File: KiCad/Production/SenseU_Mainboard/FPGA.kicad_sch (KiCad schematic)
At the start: 3 parts

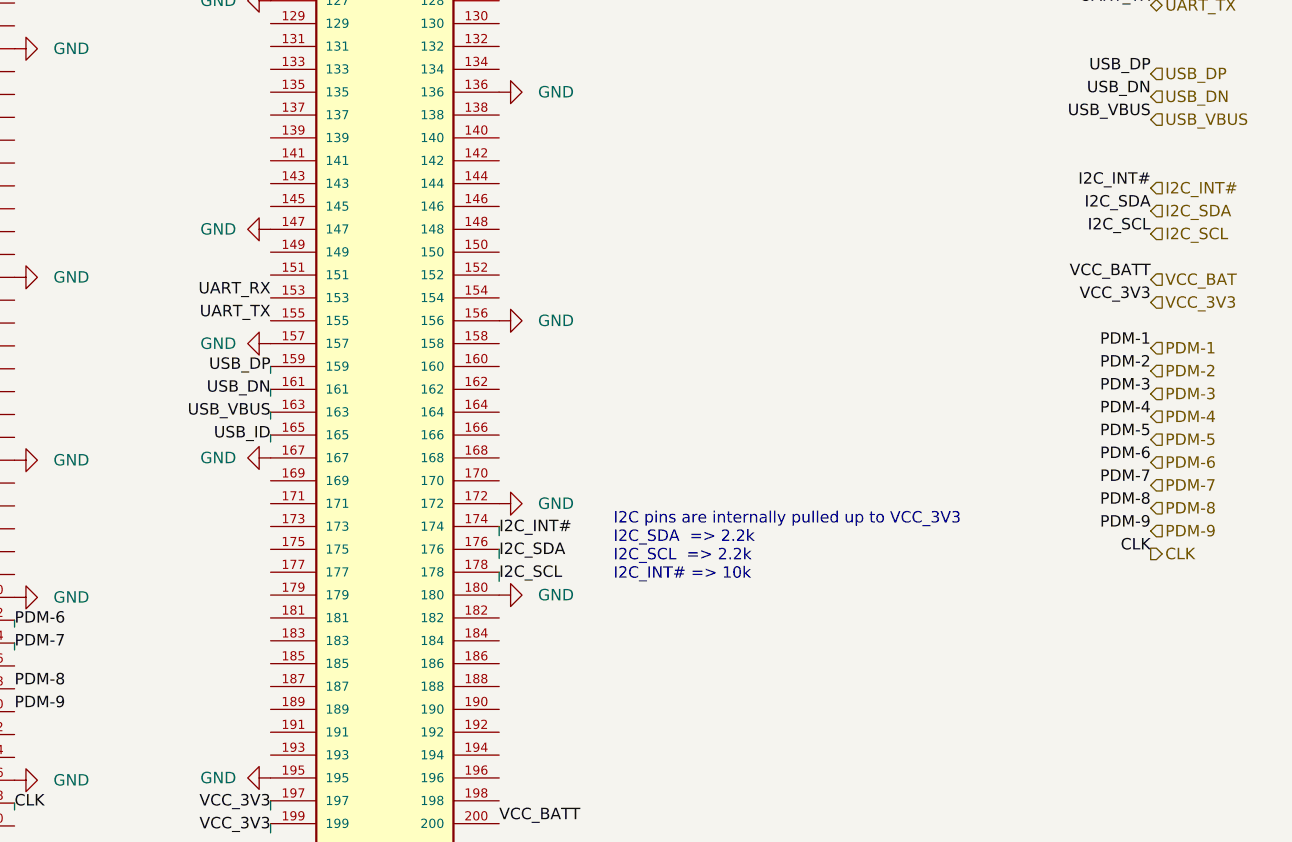
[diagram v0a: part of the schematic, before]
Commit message: added USB TO UART
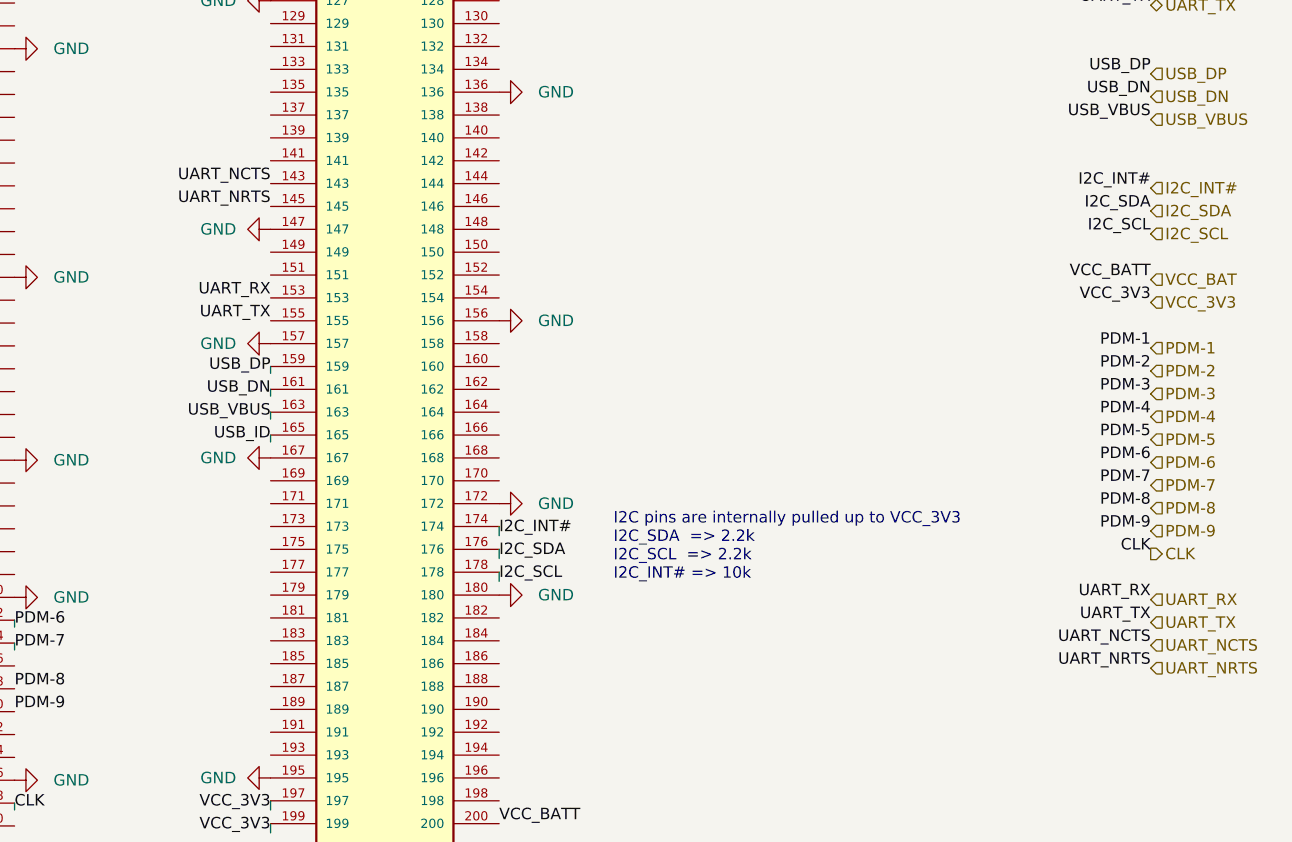
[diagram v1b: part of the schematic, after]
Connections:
- net UART_NCTS: now reaches J?.143
- net UART_NRTS: now reaches J?.145
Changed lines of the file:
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@@
+    (effects (font (size 1.27 1.27)) (justify right bottom))
+  )
+  (label "UART_NRTS" (at 163.83 73.152 180) (fields_autoplaced)
     (effects (font (size 1.27 1.27)) (justify right bottom))
   )
@@
     (effects (font (size 1.27 1.27)) (justify right bottom))
   )
+  (label "UART_TX" (at 261.62 119.38 180) (fields_autoplaced)
+    (effects (font (size 1.27 1.27)) (justify right bottom))
+  )
   (label "VCC_BATT" (at 189.23 141.732 0) (fields_autoplaced)
     (effects (font (size 1.27 1.27)) (justify left bottom))
@@
     (effects (font (size 1.27 1.27)) (justify left bottom))
   )
+  (label "UART_NCTS" (at 261.62 121.92 180) (fields_autoplaced)
+    (effects (font (size 1.27 1.27)) (justify right bottom))
+  )
   (label "VCC_3V3" (at 42.164 77.978 180) (fields_autoplaced)
     (effects (font (size 1.27 1.27)) (justify right bottom))
@@
     (effects (font (size 1.27 1.27)) (justify right bottom))
   )
+  (label "UART_NCTS" (at 163.83 70.612 180) (fields_autoplaced)
+    (effects (font (size 1.27 1.27)) (justify right bottom))
+  )
   (label "USB_ID" (at 163.83 99.314 180) (fields_autoplaced)
     (effects (font (size 1.27 1.27)) (justify right bottom))
@@
     (effects (font (size 1.27 1.27)) (justify right bottom))
   )
+  (label "UART_NRTS" (at 261.62 124.46 180) (fields_autoplaced)
+    (effects (font (size 1.27 1.27)) (justify right bottom))
+  )
   (label "PDM-6" (at 135.382 119.888 0) (fields_autoplaced)
     (effects (font (size 1.27 1.27)) (justify left bottom))
@@
   )
   (label "PDM-9" (at 261.62 109.22 180) (fields_autoplaced)
+    (effects (font (size 1.27 1.27)) (justify right bottom))
+  )
+  (label "UART_RX" (at 261.62 116.84 180) (fields_autoplaced)
     (effects (font (size 1.27 1.27)) (justify right bottom))
   )
@@
     (effects (font (size 1.27 1.27)) (justify left))
   )
+  (hierarchical_label "UART_NCTS" (shape input) (at 261.62 121.92 0) (fields_autoplaced)
+    (effects (font (size 1.27 1.27)) (justify left))
+  )
   (hierarchical_label "PDM-3" (shape input) (at 261.62 93.98 0) (fields_autoplaced)
     (effects (font (size 1.27 1.27)) (justify left))
@@
     (effects (font (size 1.27 1.27)) (justify left))
   )
+  (hierarchical_label "UART_TX" (shape input) (at 261.62 119.38 0) (fields_autoplaced)
+    (effects (font (size 1.27 1.27)) (justify left))
+  )
   (hierarchical_label "PDM-7" (shape input) (at 261.62 104.14 0) (fields_autoplaced)
     (effects (font (size 1.27 1.27)) (justify left))
@@
     (effects (font (size 1.27 1.27)) (justify left))
   )
+  (hierarchical_label "UART_RX" (shape input) (at 261.62 116.84 0) (fields_autoplaced)
+    (effects (font (size 1.27 1.27)) (justify left))
+  )
   (hierarchical_label "UART_RX" (shape bidirectional) (at 261.62 48.26 0) (fields_autoplaced)
     (effects (font (size 1.27 1.27)) (justify left))
@@
     (effects (font (size 1.27 1.27)) (justify left))
   )
+  (hierarchical_label "UART_NRTS" (shape input) (at 261.62 124.46 0) (fields_autoplaced)
+    (effects (font (size 1.27 1.27)) (justify left))
+  )

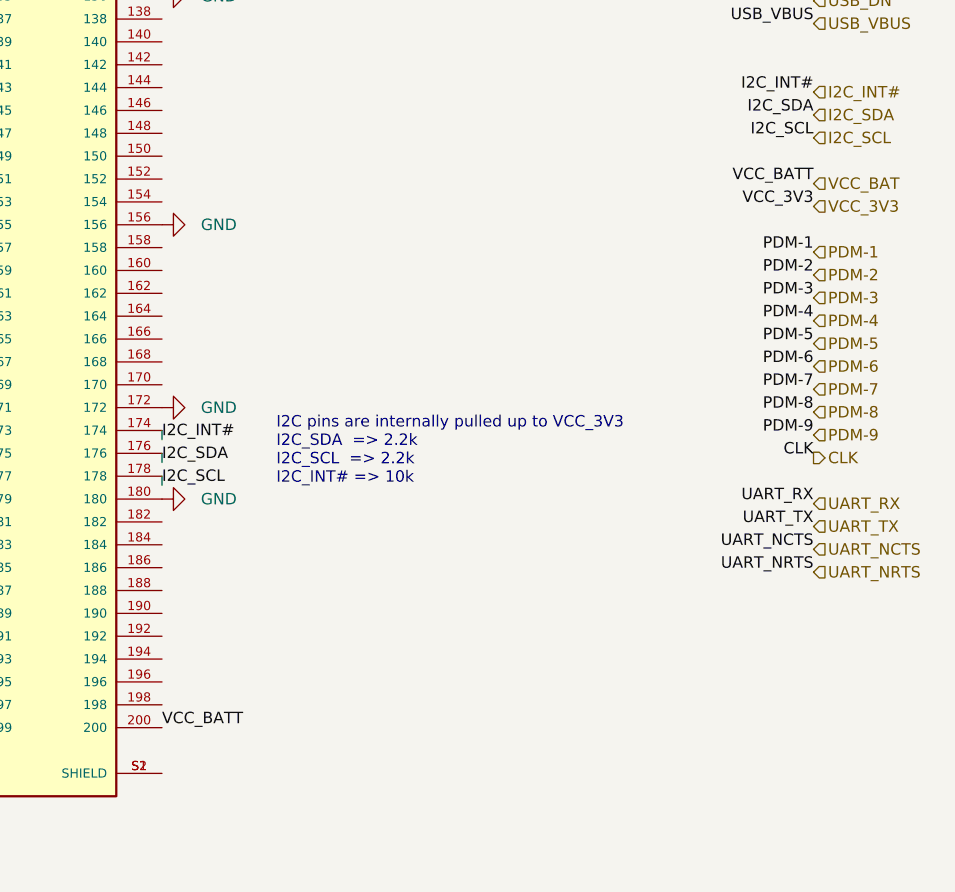
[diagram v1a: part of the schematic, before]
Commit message: removed batt co to fpga and added switch
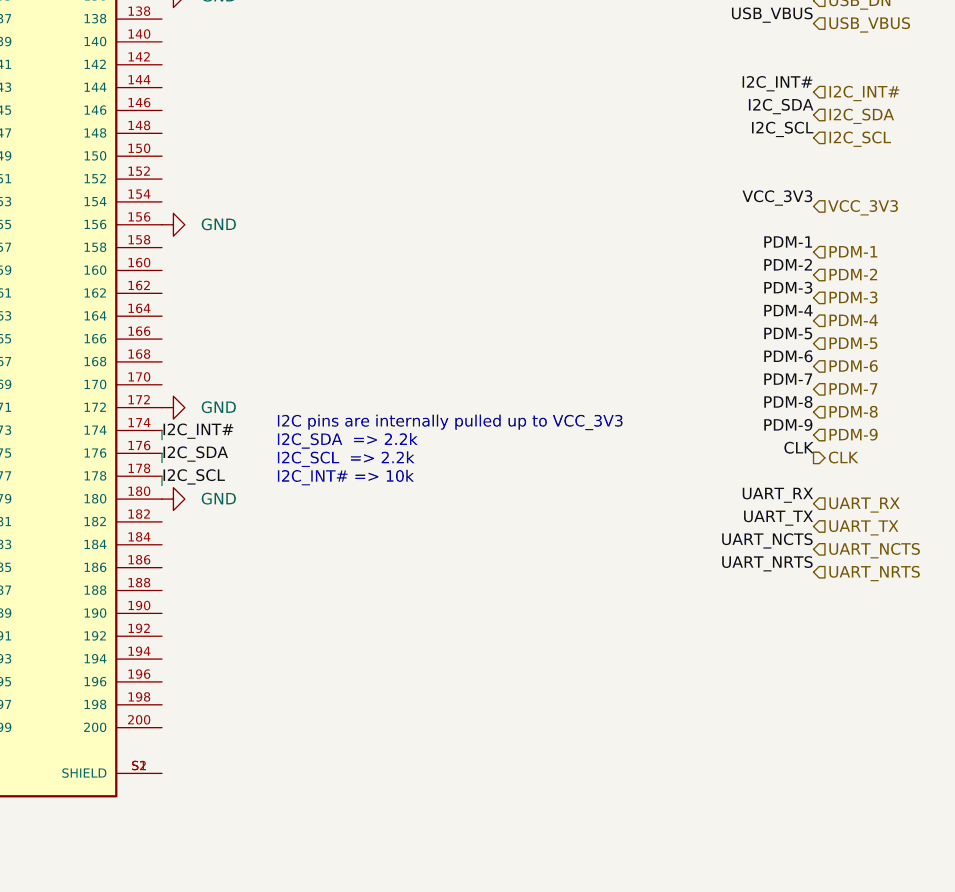
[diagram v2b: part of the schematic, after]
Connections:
- net VCC_BAT: no longer names the net of J?.200
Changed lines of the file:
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@@
     (effects (font (size 1.27 1.27)) (justify right bottom))
-  )
-  (label "VCC_BATT" (at 189.23 141.732 0) (fields_autoplaced)
-    (effects (font (size 1.27 1.27)) (justify left bottom))
   )
   (label "CLK" (at 135.382 140.208 0) (fields_autoplaced)
@@
     (effects (font (size 1.27 1.27)) (justify right bottom))
   )
-  (label "VCC_BATT" (at 261.62 81.28 180) (fields_autoplaced)
-    (effects (font (size 1.27 1.27)) (justify right bottom))
-  )
   (label "CLK" (at 261.62 111.76 180) (fields_autoplaced)
     (effects (font (size 1.27 1.27)) (justify right bottom))
@@
     (effects (font (size 1.27 1.27)) (justify left))
   )
-  (hierarchical_label "VCC_BAT" (shape input) (at 261.62 81.28 0) (fields_autoplaced)
-    (effects (font (size 1.27 1.27)) (justify left))
-  )

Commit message: routing SenseU done
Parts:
- J? (x3): footprint TE_1717254-4 -> Dimm200:TE_1717254-4
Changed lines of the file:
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@@
       (effects (font (size 1.27 1.27)))
     )
-    (property "Footprint" "TE_1717254-4" (at 122.682 91.186 0)
+    (property "Footprint" "Dimm200:TE_1717254-4" (at 122.682 91.186 0)
       (effects (font (size 1.27 1.27)) (justify bottom) hide)
     )
@@
       (effects (font (size 1.27 1.27)))
     )
-    (property "Footprint" "TE_1717254-4" (at 176.53 93.472 0)
+    (property "Footprint" "Dimm200:TE_1717254-4" (at 176.53 93.472 0)
       (effects (font (size 1.27 1.27)) (justify bottom) hide)
     )
@@
       (effects (font (size 1.27 1.27)))
     )
-    (property "Footprint" "TE_1717254-4" (at 54.864 100.838 0)
-      (effects (font (size 1.27 1.27)) (justify bottom) hide)
-    )
+    (property "Footprint" "Dimm200:TE_1717254-4" (at 54.864 100.838 0)
+      (effects (font (size 1.27 1.27)) (justify bottom) hide)
+    )
